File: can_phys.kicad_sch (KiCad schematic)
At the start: 16 parts, among them J7 Body 120R, J8 Hldx 120R, U8 TJA1051T-3, U9 TJA1051T-3

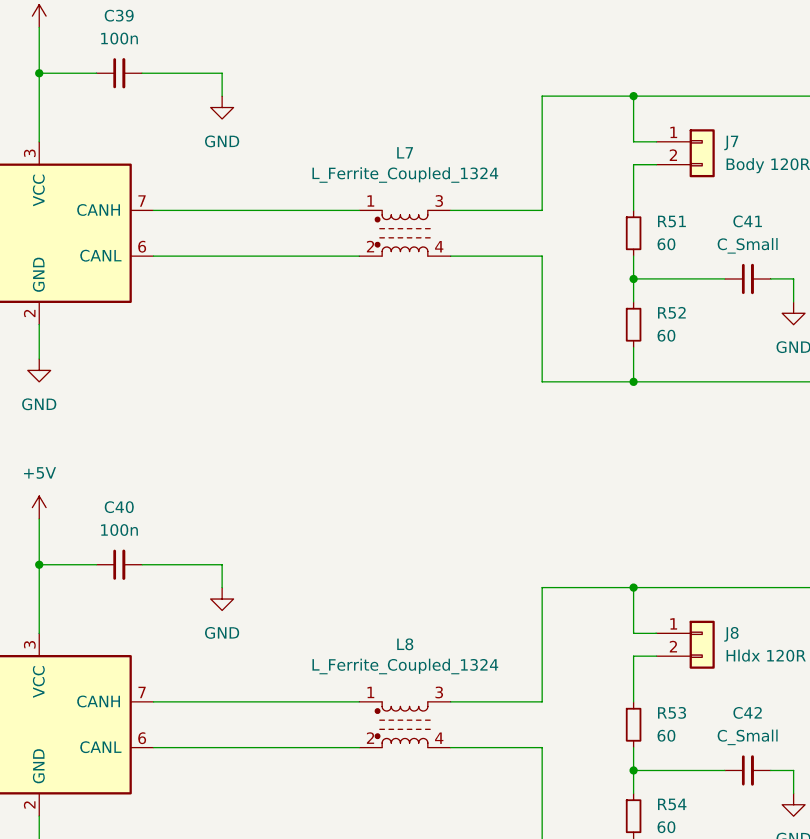
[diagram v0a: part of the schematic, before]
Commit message: sch: fixing component footprints
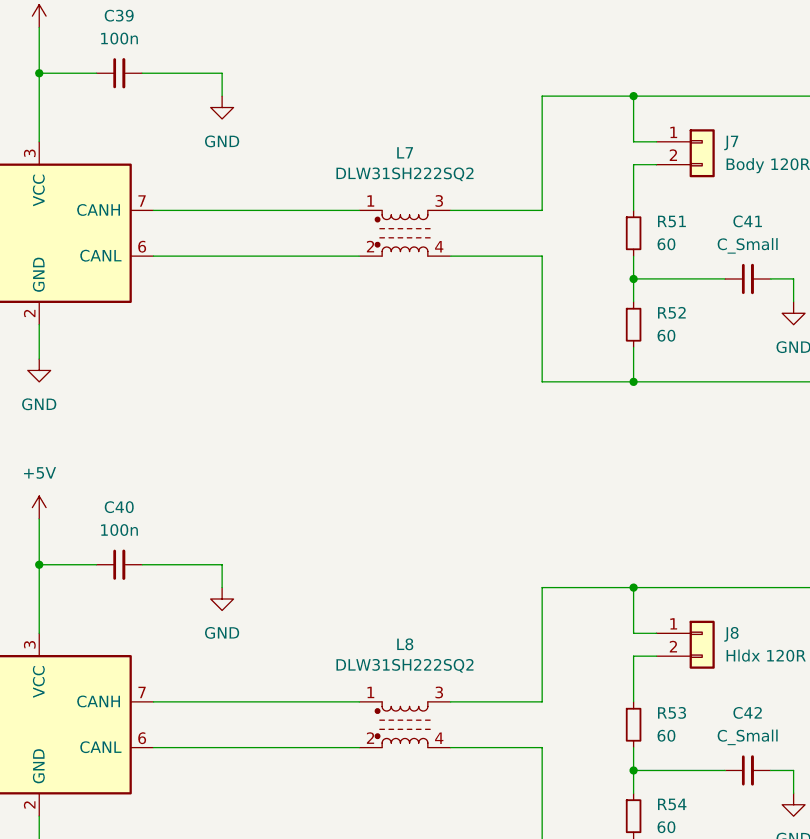
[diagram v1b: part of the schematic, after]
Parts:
- L7, L8: value L_Ferrite_Coupled_1324 -> DLW31SH222SQ2; footprint (none) -> DLW31SH222SQ2:DLW31SH222SQ2L
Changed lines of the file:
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@@
 			)
 		)
-		(property "Value" "L_Ferrite_Coupled_1324"
+		(property "Value" "DLW31SH222SQ2"
 			(at 170.18 64.516 0)
 			(effects
@@
 			)
 		)
-		(property "Footprint" ""
+		(property "Footprint" "DLW31SH222SQ2:DLW31SH222SQ2L"
 			(at 170.18 71.12 0)
 			(effects
@@
 			)
 		)
-		(property "Value" "L_Ferrite_Coupled_1324"
+		(property "Value" "DLW31SH222SQ2"
 			(at 170.18 119.126 0)
 			(effects
@@
 			)
 		)
-		(property "Footprint" ""
+		(property "Footprint" "DLW31SH222SQ2:DLW31SH222SQ2L"
 			(at 170.18 125.73 0)
 			(effects

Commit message: working on component placement
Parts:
- L7, L8: symbol Device:L_Ferrite_Coupled_1324 -> Device:L_Ferrite_Coupled_1243
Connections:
- net BODY_CAN_L: now also L7.2; no longer L7.4
- net HLDX_CAN_L: now also L8.2; no longer L8.4
- net at L7.1: now also U8.6 (CANL); no longer U8.7 (CANH)
- net at U9.6 (CANL): now also L8.1; no longer L8.2
- net at U9.7 (CANH): now also L8.4; no longer L8.1
- new net: L7.4, U8.7 (CANH)
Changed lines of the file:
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@@
 	)
 	(symbol
-		(lib_id "Device:L_Ferrite_Coupled_1324")
+		(lib_id "Device:L_Ferrite_Coupled_1243")
 		(at 170.18 71.12 0)
+		(mirror x)
 		(unit 1)
 		(exclude_from_sim no)
@@
 		(dnp no)
 		(property "Reference" "L7"
-			(at 170.18 62.23 0)
+			(at 170.18 80.01 0)
 			(effects
 				(font
@@
 		)
 		(property "Value" "DLW31SH222SQ2"
-			(at 170.18 64.516 0)
+			(at 170.18 77.724 0)
 			(effects
 				(font
@@
 			)
 		)
-		(property "Datasheet" "~"
+		(property "Datasheet" "https://www.mouser.it/datasheet/2/281/DLW31SH222SQ2_23-1915424.pdf"
 			(at 170.18 71.12 0)
 			(effects
@@
 	)
 	(symbol
-		(lib_id "Device:L_Ferrite_Coupled_1324")
+		(lib_id "Device:L_Ferrite_Coupled_1243")
 		(at 170.18 125.73 0)
+		(mirror x)
 		(unit 1)
 		(exclude_from_sim no)
@@
 		(dnp no)
 		(property "Reference" "L8"
-			(at 170.18 116.84 0)
+			(at 170.18 134.62 0)
 			(effects
 				(font
@@
 		)
 		(property "Value" "DLW31SH222SQ2"
-			(at 170.18 119.126 0)
+			(at 170.18 132.334 0)
 			(effects
 				(font
@@
 			)
 		)
-		(property "Datasheet" "~"
+		(property "Datasheet" "https://www.mouser.it/datasheet/2/281/DLW31SH222SQ2_23-1915424.pdf"
 			(at 170.18 125.73 0)
 			(effects
